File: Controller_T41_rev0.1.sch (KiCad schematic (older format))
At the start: 23 parts, among them J1 RJ45, J2 RJ45, J3 RJ45, J4 RJ45, J5 RJ45, J6 RJ45, J7 RJ45, J8 RJ45, J9 Screw_Terminal_01x02, U1 74HC245, U2 74HC245, U3 Teensy4.1, U4 74HC245, U5 74HC245

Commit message: updated board layout, converted rj-45 ports to dual rj-45 ports Converted design to kicad 5.
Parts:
- removed J1, J2, J3, J4, J5, J6, J7, J8: RJ45, Connector_RJ:RJ45_Amphenol_54602-x08_Horizontal, symbol Connector:RJ45
- added J1, J2, J3, J4: RJ45_LED_Shielded_x2, Connector_RJ:RJ45_Amphenol_RJHSE538X-02, symbol Connector:RJ45_LED_Shielded_x2
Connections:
- wire segments 282 -> 301
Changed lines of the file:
@@
 EESchema Schematic File Version 4
-LIBS:Controller_T41_rev0.1-cache
 EELAYER 30 0
 EELAYER END
@@
 Wire Wire Line
 	4150 3690 4450 3690
-$Comp
-L Connector:RJ45 J4
-U 1 1 5F9D3F0E
-P 1610 5450
-F 0 "J4" H 1667 6117 50  0000 C CNN
-F 1 "RJ45" H 1667 6026 50  0000 C CNN
-F 2 "Connector_RJ:RJ45_Amphenol_54602-x08_Horizontal" V 1610 5475 50  0001 C CNN
-F 3 "~" V 1610 5475 50  0001 C CNN
-	1    1610 5450
-	1    0    0    -1
-$EndComp
-$Comp
-L Connector:RJ45 J3
-U 1 1 5F9D7554
-P 1580 4420
-F 0 "J3" H 1637 5087 50  0000 C CNN
-F 1 "RJ45" H 1637 4996 50  0000 C CNN
-F 2 "Connector_RJ:RJ45_Amphenol_54602-x08_Horizontal" V 1580 4445 50  0001 C CNN
-F 3 "~" V 1580 4445 50  0001 C CNN
-	1    1580 4420
-	1    0    0    -1
-$EndComp
-$Comp
-L Connector:RJ45 J2
-U 1 1 5F9D9E52
-P 1580 3390
-F 0 "J2" H 1637 4057 50  0000 C CNN
-F 1 "RJ45" H 1637 3966 50  0000 C CNN
-F 2 "Connector_RJ:RJ45_Amphenol_54602-x08_Horizontal" V 1580 3415 50  0001 C CNN
-F 3 "~" V 1580 3415 50  0001 C CNN
-	1    1580 3390
-	1    0    0    -1
-$EndComp
-$Comp
-L Connector:RJ45 J1
-U 1 1 5F9DAF98
-P 1580 2350
-F 0 "J1" H 1637 3017 50  0000 C CNN
-F 1 "RJ45" H 1637 2926 50  0000 C CNN
-F 2 "Connector_RJ:RJ45_Amphenol_54602-x08_Horizontal" V 1580 2375 50  0001 C CNN
-F 3 "~" V 1580 2375 50  0001 C CNN
-	1    1580 2350
-	1    0    0    -1
-$EndComp
 Wire Wire Line
 	2440 5110 2440 5650
@@
 	2440 4020 1980 4020
 Wire Wire Line
-	1980 3590 2990 3590
-Wire Wire Line
-	2990 3490 2110 3490
-Wire Wire Line
-	2110 3490 2110 3390
-Wire Wire Line
-	2110 3390 1980 3390
-Wire Wire Line
 	1980 3190 2140 3190
 Wire Wire Line
-	2140 3190 2140 3390
-Wire Wire Line
-	2140 3390 2990 3390
-Wire Wire Line
-	2990 3290 2160 3290
-Wire Wire Line
-	2160 3290 2160 2990
-Wire Wire Line
 	2160 2990 1980 2990
 Wire Wire Line
@@
 Wire Wire Line
 	2640 2890 2640 1950
-Wire Wire Line
-	2640 1950 2370 1950
 $Comp
 L power:GND #PWR0101
@@
 Connection ~ 2100 5750
 Wire Wire Line
-	2100 5750 2100 6630
-Wire Wire Line
 	2010 5550 2100 5550
 Wire Wire Line
@@
 Connection ~ 2100 4720
 Wire Wire Line
-	2100 4720 2100 5150
+	2100 4720 2100 4920
 Wire Wire Line
 	1980 2250 2100 2250
@@
 	1980 3090 2100 3090
 Wire Wire Line
-	2100 2650 2100 3090
+	2100 2650 2100 2850
 Connection ~ 2100 3090
 Wire Wire Line
@@
 Connection ~ 2100 3290
 Wire Wire Line
-	1980 3490 2100 3490
-Wire Wire Line
-	2100 3290 2100 3490
-Connection ~ 2100 3490
-Wire Wire Line
 	1980 3690 2100 3690
-Wire Wire Line
-	2100 3490 2100 3690
 Connection ~ 2100 3690
 Wire Wire Line
-	2100 3690 2100 3950
+	2100 3690 2100 3890
 Wire Wire Line
 	8590 4810 8590 5730
@@
 	8590 3990 8590 4110
 Wire Wire Line
-	8140 3190 8140 3470
-Wire Wire Line
-	8140 3470 9290 3470
-Wire Wire Line
-	9290 3270 8180 3270
-Wire Wire Line
-	8180 3270 8180 3090
-Wire Wire Line
-	8180 3090 8140 3090
-Wire Wire Line
-	8140 2990 8240 2990
-Wire Wire Line
-	8240 2990 8240 3070
-Wire Wire Line
-	8240 3070 9290 3070
-Wire Wire Line
-	9290 2870 9200 2870
-Wire Wire Line
-	9200 2870 9200 2890
-Wire Wire Line
-	9200 2890 8140 2890
-Wire Wire Line
-	8140 2790 9250 2790
-Wire Wire Line
-	9250 2790 9250 2340
-Wire Wire Line
-	8140 2690 9170 2690
-Wire Wire Line
-	9170 2690 9170 2140
-Wire Wire Line
 	9170 2140 9250 2140
 Wire Wire Line
 	9250 1940 9060 1940
-Wire Wire Line
-	9060 1940 9060 2590
-Wire Wire Line
-	9060 2590 8140 2590
-Wire Wire Line
-	8140 2490 9020 2490
-Wire Wire Line
-	9020 2490 9020 1740
 Wire Wire Line
 	9020 1740 9250 1740
@@
 Connection ~ 9190 4490
 Wire Wire Line
-	9190 4490 9190 5030
+	9190 4490 9190 4830
 Wire Wire Line
 	9310 4290 9190 4290
@@
 Wire Wire Line
 	9290 2770 9190 2770
-Wire Wire Line
-	9190 2240 9190 2770
 Connection ~ 9190 2770
 Wire Wire Line
@@
 Connection ~ 9190 3510
 Wire Wire Line
-	9190 3510 9190 3890
+	9190 3510 9190 3690
 Connection ~ 3340 6630
 Wire Wire Line
@@
 	8530 1890 8900 1890
 Wire Wire Line
-	2370 1530 2370 1950
-Connection ~ 2370 1950
-Wire Wire Line
-	2370 1950 1980 1950
-Wire Wire Line
 	6440 1660 3890 1660
 Wire Wire Line
@@
 	9290 2980 9290 2970
 $Comp
-L Connector:RJ45 J5
-U 1 1 5F9E44CF
+L Connector:RJ45_LED_Shielded_x2 J4
+U 2 1 5FA62167
 P 9650 1940
-F 0 "J5" H 9320 1944 50  0000 R CNN
-F 1 "RJ45" H 9320 2035 50  0000 R CNN
-F 2 "Connector_RJ:RJ45_Amphenol_54602-x08_Horizontal" V 9650 1965 50  0001 C CNN
+F 0 "J4" H 9650 2607 50  0000 C CNN
+F 1 "RJ45_LED_Shielded_x2" H 9650 2516 50  0000 C CNN
+F 2 "Connector_RJ:RJ45_Amphenol_RJHSE538X-02" V 9650 1965 50  0001 C CNN
 F 3 "~" V 9650 1965 50  0001 C CNN
-	1    9650 1940
+	2    9650 1940
 	-1   0    0    1
 $EndComp
 $Comp
-L Connector:RJ45 J6
-U 1 1 5F9E3680
+L Connector:RJ45_LED_Shielded_x2 J4
+U 1 1 5FA95E4A
 P 9690 3070
-F 0 "J6" H 9360 3074 50  0000 R CNN
-F 1 "RJ45" H 9360 3165 50  0000 R CNN
-F 2 "Connector_RJ:RJ45_Amphenol_54602-x08_Horizontal" V 9690 3095 50  0001 C CNN
+F 0 "J4" H 9690 3737 50  0000 C CNN
+F 1 "RJ45_LED_Shielded_x2" H 9690 3646 50  0000 C CNN
+F 2 "Connector_RJ:RJ45_Amphenol_RJHSE538X-02" V 9690 3095 50  0001 C CNN
 F 3 "~" V 9690 3095 50  0001 C CNN
 	1    9690 3070
@@
 $EndComp
 $Comp
-L Connector:RJ45 J7
-U 1 1 5F9E13FA
+L Connector:RJ45_LED_Shielded_x2 J1
+U 1 1 5FB4DD27
+P 1580 2350
+F 0 "J1" H 1580 3017 50  0000 C CNN
+F 1 "RJ45_LED_Shielded_x2" H 1580 2926 50  0000 C CNN
+F 2 "Connector_RJ:RJ45_Amphenol_RJHSE538X-02" V 1580 2375 50  0001 C CNN
+F 3 "~" V 1580 2375 50  0001 C CNN
+	1    1580 2350
+	1    0    0    -1
+$EndComp
+$Comp
+L Connector:RJ45_LED_Shielded_x2 J1
+U 2 1 5FB50B78
+P 1580 3390
+F 0 "J1" H 1580 4057 50  0000 C CNN
+F 1 "RJ45_LED_Shielded_x2" H 1580 3966 50  0000 C CNN
+F 2 "Connector_RJ:RJ45_Amphenol_RJHSE538X-02" V 1580 3415 50  0001 C CNN
+F 3 "~" V 1580 3415 50  0001 C CNN
+	2    1580 3390
+	1    0    0    -1
+$EndComp
+$Comp
+L Connector:RJ45_LED_Shielded_x2 J2
+U 2 1 5FC295D6
+P 1580 4420
+F 0 "J2" H 1580 5087 50  0000 C CNN
+F 1 "RJ45_LED_Shielded_x2" H 1580 4996 50  0000 C CNN
+F 2 "Connector_RJ:RJ45_Amphenol_RJHSE538X-02" V 1580 4445 50  0001 C CNN
+F 3 "~" V 1580 4445 50  0001 C CNN
+	2    1580 4420
+	1    0    0    -1
+$EndComp
+$Comp
+L Connector:RJ45_LED_Shielded_x2 J2
+U 1 1 5FC2B90B
+P 1610 5450
+F 0 "J2" H 1610 6117 50  0000 C CNN
+F 1 "RJ45_LED_Shielded_x2" H 1610 6026 50  0000 C CNN
+F 2 "Connector_RJ:RJ45_Amphenol_RJHSE538X-02" V 1610 5475 50  0001 C CNN
+F 3 "~" V 1610 5475 50  0001 C CNN
+	1    1610 5450
+	1    0    0    -1
+$EndComp
+$Comp
+L Connector:RJ45_LED_Shielded_x2 J3
+U 2 1 5FC36180
+P 9770 5330
+F 0 "J3" H 9770 5997 50  0000 C CNN
+F 1 "RJ45_LED_Shielded_x2" H 9770 5906 50  0000 C CNN
+F 2 "Connector_RJ:RJ45_Amphenol_RJHSE538X-02" V 9770 5355 50  0001 C CNN
+F 3 "~" V 9770 5355 50  0001 C CNN
+	2    9770 5330
+	-1   0    0    1
+$EndComp
+$Comp
+L Connector:RJ45_LED_Shielded_x2 J3
+U 1 1 5FC36186
 P 9710 4190
-F 0 "J7" H 9380 4194 50  0000 R CNN
-F 1 "RJ45" H 9380 4285 50  0000 R CNN
-F 2 "Connector_RJ:RJ45_Amphenol_54602-x08_Horizontal" V 9710 4215 50  0001 C CNN
+F 0 "J3" H 9710 4857 50  0000 C CNN
+F 1 "RJ45_LED_Shielded_x2" H 9710 4766 50  0000 C CNN
+F 2 "Connector_RJ:RJ45_Amphenol_RJHSE538X-02" V 9710 4215 50  0001 C CNN
 F 3 "~" V 9710 4215 50  0001 C CNN
 	1    9710 4190
 	-1   0    0    1
 $EndComp
-$Comp
-L Connector:RJ45 J8
-U 1 1 5F9DC7E0
-P 9770 5330
-F 0 "J8" H 9440 5334 50  0000 R CNN
-F 1 "RJ45" H 9440 5425 50  0000 R CNN
-F 2 "Connector_RJ:RJ45_Amphenol_54602-x08_Horizontal" V 9770 5355 50  0001 C CNN
-F 3 "~" V 9770 5355 50  0001 C CNN
-	1    9770 5330
-	-1   0    0    1
-$EndComp
+Wire Wire Line
+	1980 1950 2640 1950
+Wire Wire Line
+	2370 1530 2370 2050
+Wire Wire Line
+	2370 2050 2100 2050
+Connection ~ 2100 2050
+Wire Wire Line
+	2100 3290 2100 3490
+Wire Wire Line
+	2160 2990 2160 3590
+Wire Wire Line
+	2990 3490 2140 3490
+Wire Wire Line
+	2140 3190 2140 3490
+Wire Wire Line
+	1980 3390 2990 3390
+Wire Wire Line
+	2160 3590 2990 3590
+Wire Wire Line
+	2990 3290 2460 3290
+Wire Wire Line
+	2460 3290 2460 3530
+Wire Wire Line
+	2460 3530 2060 3530
+Wire Wire Line
+	2060 3530 2060 3590
+Wire Wire Line
+	2060 3590 1980 3590
+Wire Wire Line
+	1980 3490 2100 3490
+Connection ~ 2100 3490
+Wire Wire Line
+	2100 3490 2100 3690
+Wire Wire Line
+	9190 1640 9190 1440
+Wire Wire Line
+	9190 1440 9650 1440
+Wire Wire Line
+	9690 2570 9190 2570
+Wire Wire Line
+	9190 2240 9190 2570
+Connection ~ 9190 2570
+Wire Wire Line
+	9190 2570 9190 2770
+Wire Wire Line
+	9710 3690 9190 3690
+Connection ~ 9190 3690
+Wire Wire Line
+	9190 3690 9190 3890
+Wire Wire Line
+	9770 4830 9190 4830
+Connection ~ 9190 4830
+Wire Wire Line
+	9190 4830 9190 5030
+Wire Wire Line
+	1610 5950 2100 5950
+Wire Wire Line
+	2100 5750 2100 5950
+Connection ~ 2100 5950
+Wire Wire Line
+	2100 5950 2100 6630
+Wire Wire Line
+	1580 4920 2100 4920
+Connection ~ 2100 4920
+Wire Wire Line
+	2100 4920 2100 5150
+Wire Wire Line
+	1580 3890 2100 3890
+Connection ~ 2100 3890
+Wire Wire Line
+	2100 3890 2100 3950
+Wire Wire Line
+	1580 2850 2100 2850
+Connection ~ 2100 2850
+Wire Wire Line
+	2100 2850 2100 3090
+Wire Wire Line
+	9020 1740 9020 2790
+Wire Wire Line
+	9020 2790 8140 2790
+Wire Wire Line
+	8140 2690 9060 2690
+Wire Wire Line
+	9060 2690 9060 1940
+Wire Wire Line
+	9170 2140 9170 2590
+Wire Wire Line
+	9170 2590 8140 2590
+Wire Wire Line
+	8140 2490 9130 2490
+Wire Wire Line
+	9130 2490 9130 2340
+Wire Wire Line
+	9130 2340 9250 2340
+Wire Wire Line
+	8140 2890 8460 2890
+Wire Wire Line
+	8460 2890 8460 3470
+Wire Wire Line
+	8460 3470 9290 3470
+Wire Wire Line
+	9290 3270 8590 3270
+Wire Wire Line
+	8590 3270 8590 2990
+Wire Wire Line
+	8590 2990 8140 2990
+Wire Wire Line
+	8140 3090 9290 3090
+Wire Wire Line
+	9290 3090 9290 3070
+Wire Wire Line
+	9290 2870 8760 2870
+Wire Wire Line
+	8760 2870 8760 3190
+Wire Wire Line
+	8760 3190 8140 3190
 $EndSCHEMATC

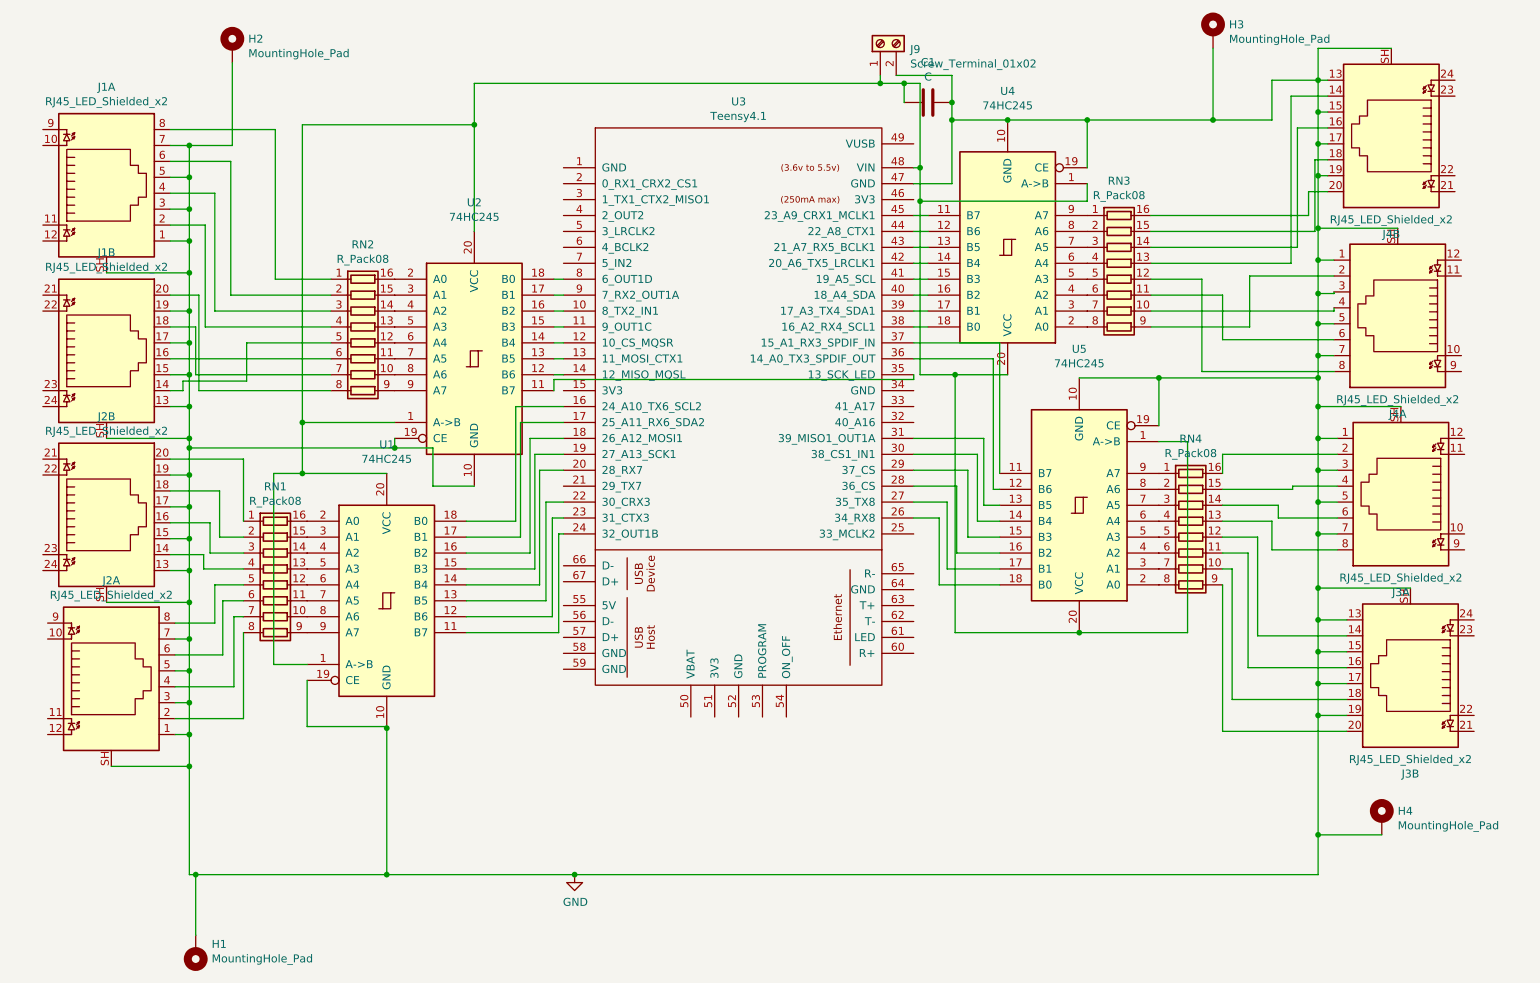
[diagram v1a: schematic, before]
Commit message: Switching to SMT components where possible
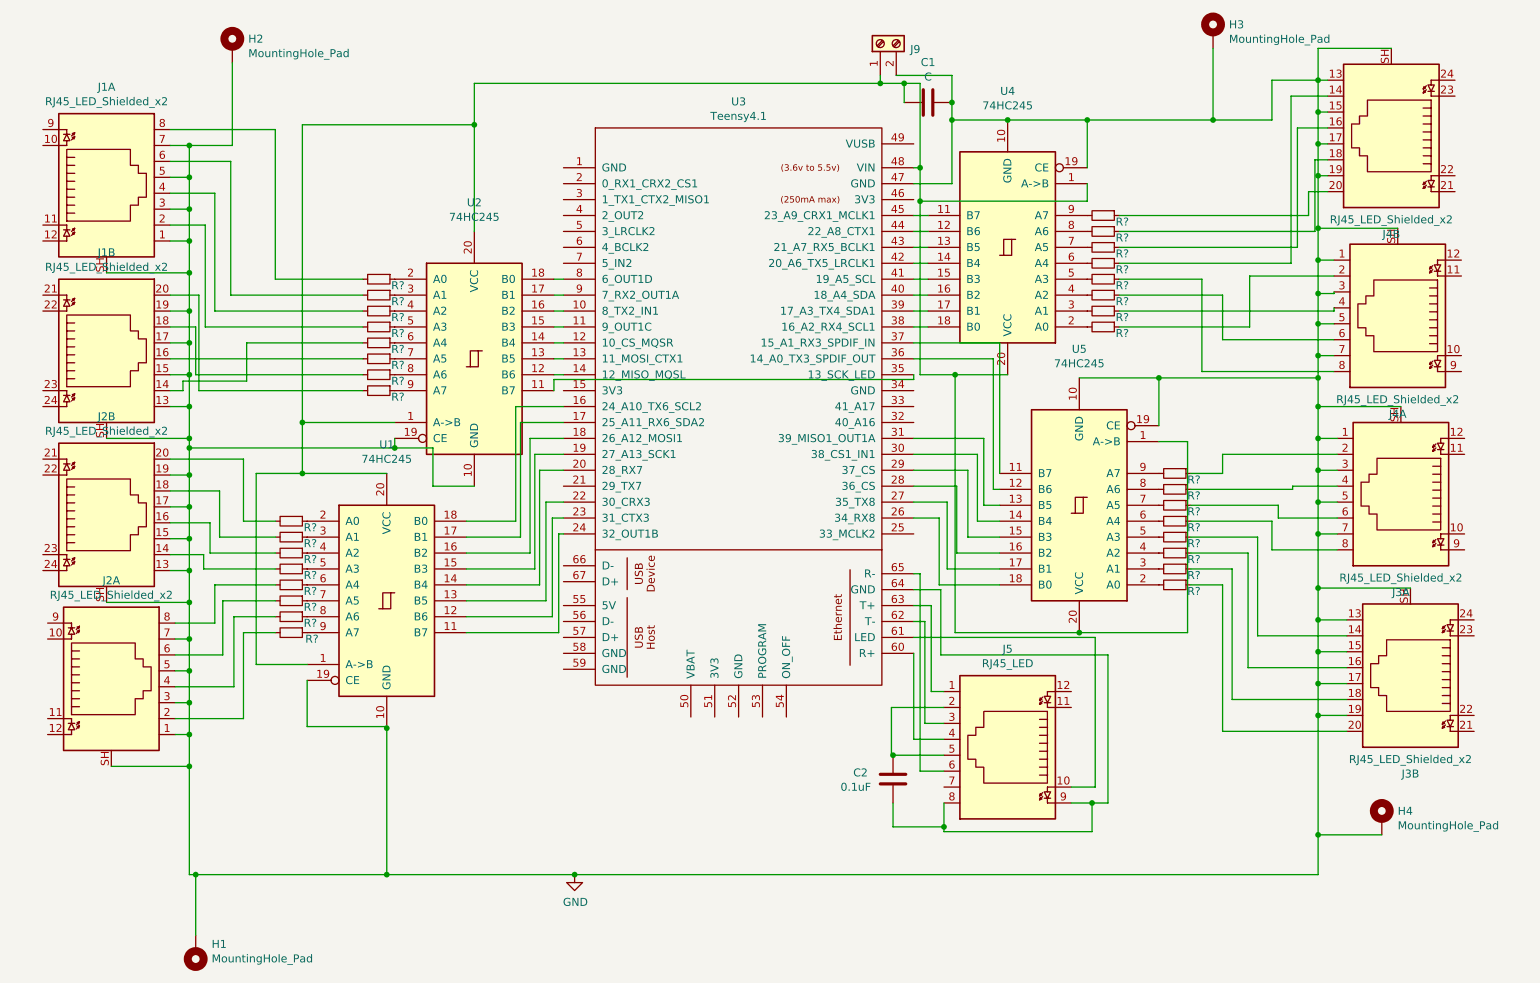
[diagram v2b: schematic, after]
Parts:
- removed RN1, RN2, RN3, RN4: R_Pack08, Package_DIP:DIP-16_W7.62mm, symbol Device:R_Pack08
- added C2: 0.1uF, Capacitor_THT:C_Disc_D5.0mm_W2.5mm_P2.50mm, symbol Device:C
- added J5: RJ45_LED, Connector_RJ:RJ45_Cetus_J1B1211CCD_Horizontal, symbol Connector:RJ45_LED
- added R? (x32): 100ohm, symbol Device:R_Small
- U1, U2, U4, U5: footprint Package_DIP:DIP-20_W7.62mm -> Package_SO:SOIC-20W_7.5x12.8mm_P1.27mm
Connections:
- net at U3.60 (R+): now also J5.4
- net at U3.61 (LED): now also J5.10
- net at U3.62 (T-): now also J5.3
- net at U3.63 (T+): now also J5.1
- net at U3.64 (GND): now also C2.2, J5.8, J5.9
- net at U3.65 (R-): now also J5.6
- net at U2.2 (A0): now also R?.1
- net at U2.3 (A1): now also R?.1
- net at U2.4 (A2): now also R?.1
- net at U2.5 (A3): now also R?.1
- net at U2.6 (A4): now also R?.1
- net at U2.7 (A5): now also R?.1
- net at U2.8 (A6): now also R?.1
- net at U2.9 (A7): now also R?.1
- net at U1.2 (A0): now also R?.1
- net at U1.3 (A1): now also R?.1
- net at U1.4 (A2): now also R?.1
- net at U1.5 (A3): now also R?.1
- net at U1.6 (A4): now also R?.1
- net at U1.7 (A5): now also R?.1
- net at U1.8 (A6): now also R?.1
- net at U1.9 (A7): now also R?.1
- net at U5.2 (A0): now also R?.2
- net at U5.3 (A1): now also R?.2
- net at U5.4 (A2): now also R?.2
- net at U5.5 (A3): now also R?.2
- net at U5.6 (A4): now also R?.2
- net at U5.7 (A5): now also R?.2
- net at U5.8 (A6): now also R?.2
- net at U5.9 (A7): now also R?.2
- net at U4.2 (A0): now also R?.2
- net at U4.3 (A1): now also R?.2
- net at U4.4 (A2): now also R?.2
- net at U4.5 (A3): now also R?.2
- net at U4.6 (A4): now also R?.2
- net at U4.7 (A5): now also R?.2
- net at U4.8 (A6): now also R?.2
- net at U4.9 (A7): now also R?.2
- net at J1.8: now also R?.2
- net at J1.6: now also R?.2
- net at J1.4: now also R?.2
- net at J1.2: now also R?.2
- net at J1.14: now also R?.2
- net at J1.16: now also R?.2
- net at J1.18: now also R?.2
- net at J1.20: now also R?.2
- net at J2.20: now also R?.2
- net at J2.18: now also R?.2
- net at J2.16: now also R?.2
- net at J2.14: now also R?.2
- net at J2.8: now also R?.2
- net at J2.6: now also R?.2
- net at J2.4: now also R?.2
- net at J2.2: now also R?.2
- net at J4.4: now also R?.1
- net at J4.6: now also R?.1
- net at J4.8: now also R?.1
- net at J4.14: now also R?.1
- net at J4.16: now also R?.1
- net at J4.18: now also R?.1
- net at J4.20: now also R?.1
- net at J4.2: now also R?.1
- net at J3.18: now also R?.1
- net at J3.16: now also R?.1
- net at J3.14: now also R?.1
- net at J3.8: now also R?.1
- net at J3.6: now also R?.1
- net at J3.4: now also R?.1
- net at J3.2: now also R?.1
- net at J3.20: now also R?.1
- new net: C2.1, J5.2, J5.5
